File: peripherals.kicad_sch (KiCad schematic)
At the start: 9 parts

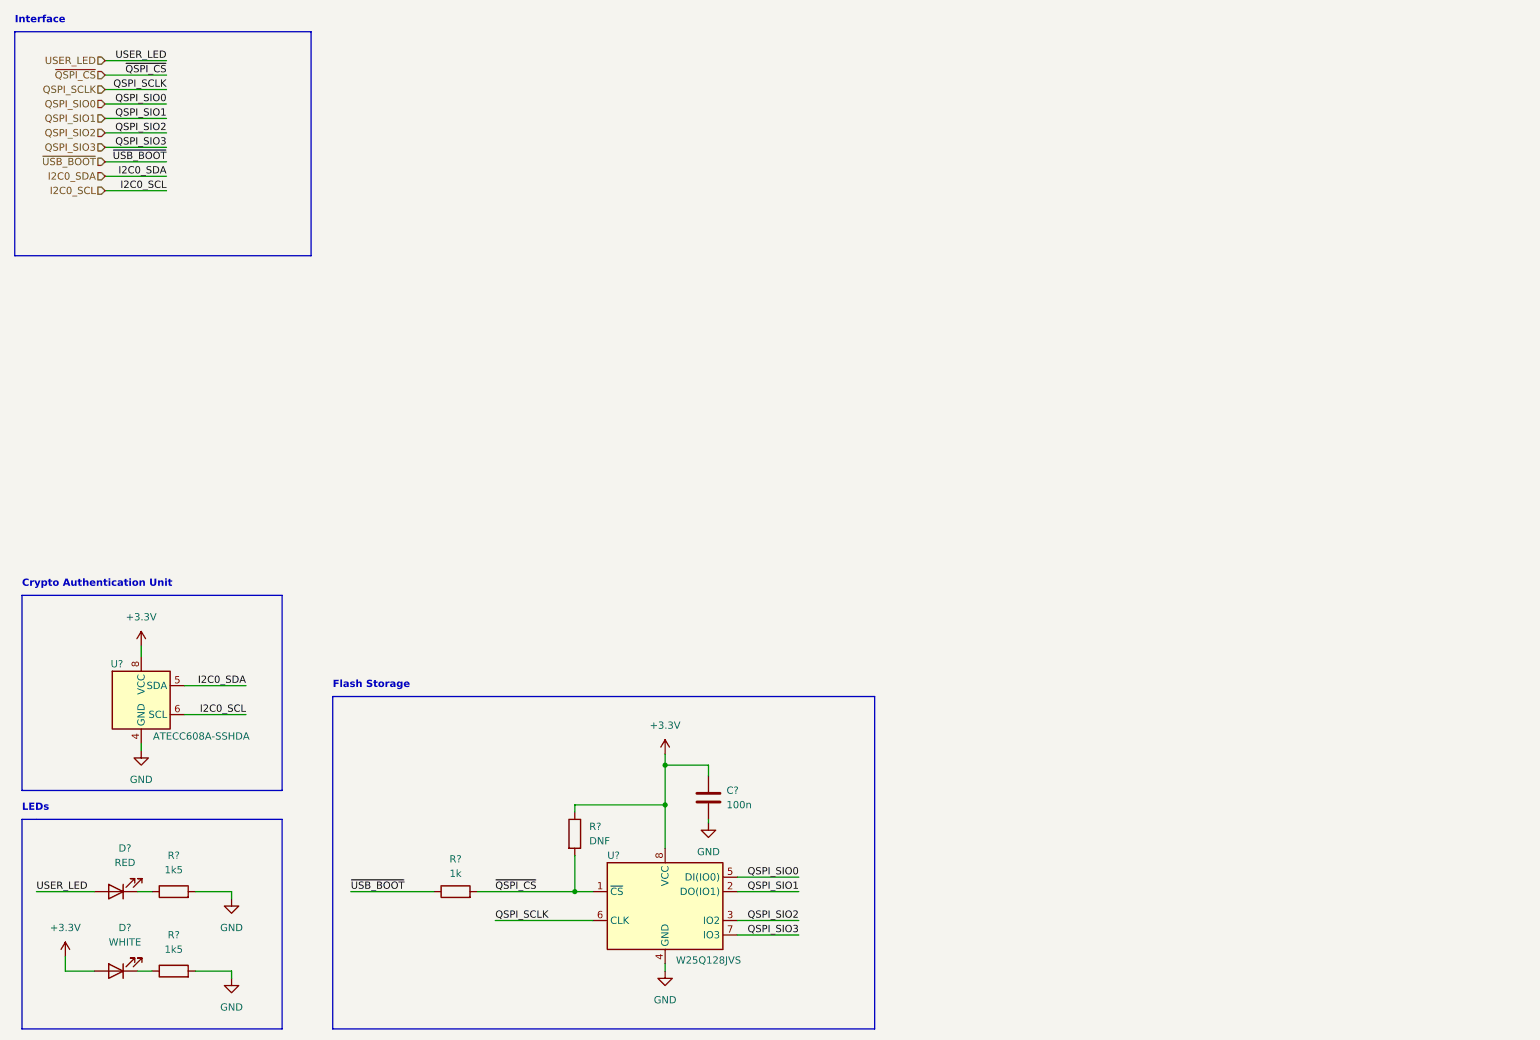
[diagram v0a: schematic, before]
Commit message: All component except led matrix
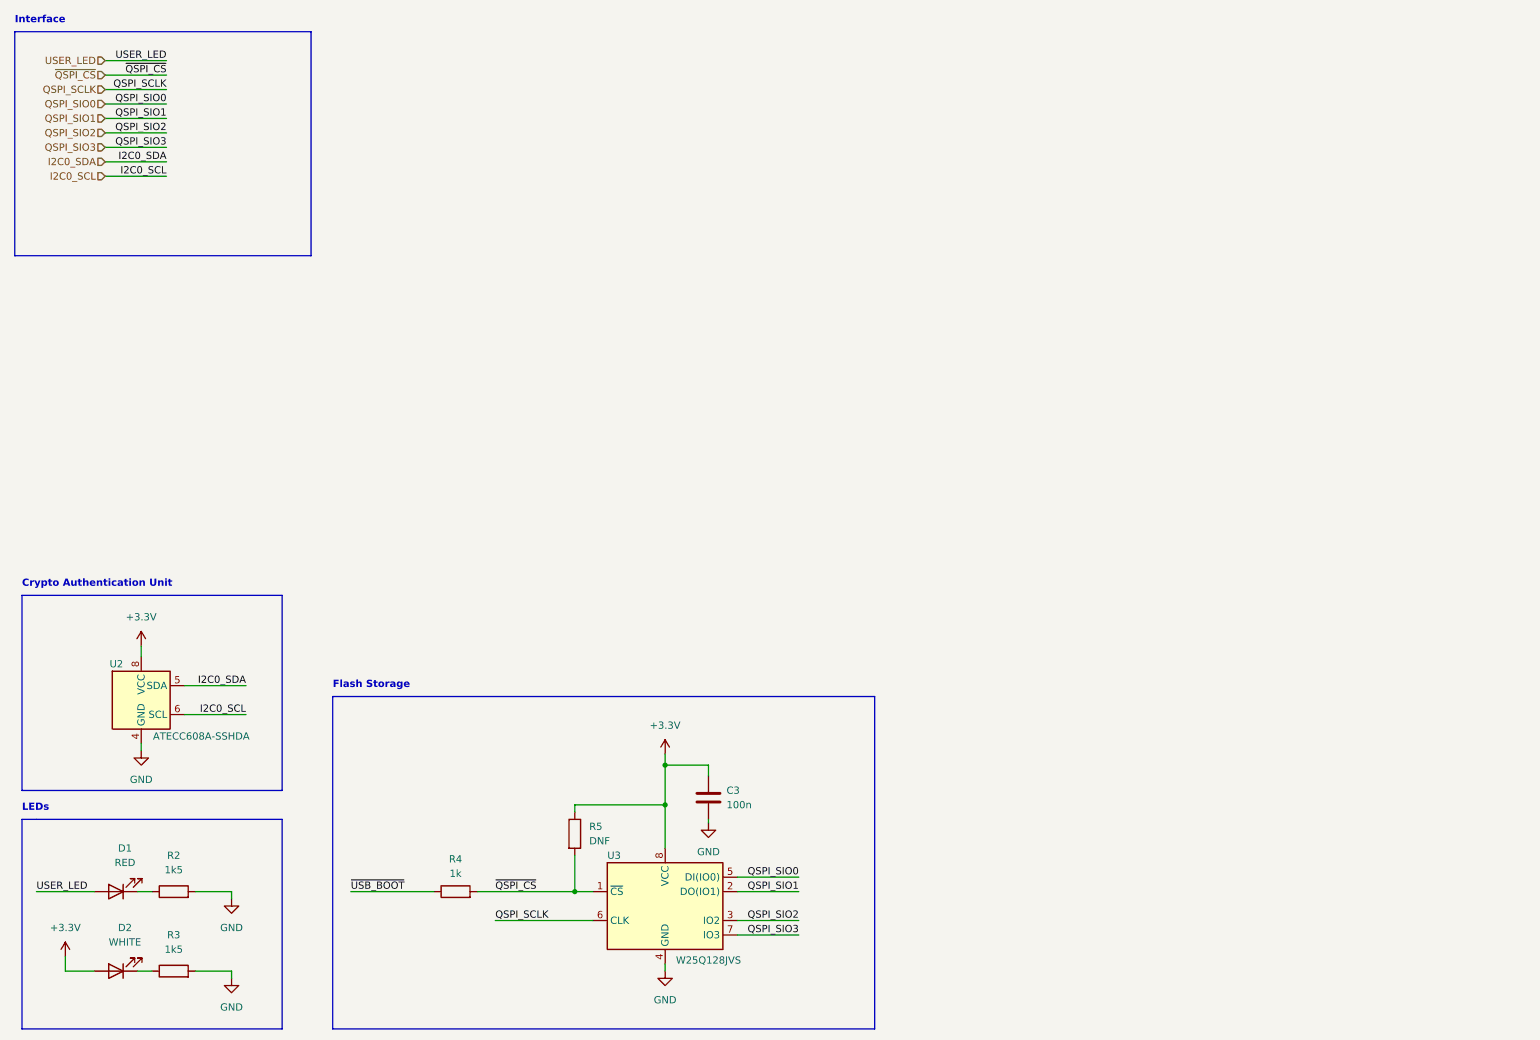
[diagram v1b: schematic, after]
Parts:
- gave numbers to parts that had none: 9
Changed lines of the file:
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@@
+    (stroke (width 0) (type default) (color 0 0 0 0))
+  )
+  (wire (pts (xy 31.115 41.91) (xy 41.91 41.91))
+    (stroke (width 0) (type default) (color 0 0 0 0))
+  )
+  (wire (pts (xy 31.115 39.37) (xy 41.91 39.37))
     (stroke (width 0) (type default) (color 0 0 0 0))
   )
@@
     (stroke (width 0) (type default) (color 0 0 0 0))
   )
-  (wire (pts (xy 31.115 39.37) (xy 41.91 39.37))
-    (stroke (width 0) (type default) (color 0 0 0 0))
-  )
-  (wire (pts (xy 31.115 46.99) (xy 41.91 46.99))
-    (stroke (width 0) (type default) (color 0 0 0 0))
-  )
   (wire (pts (xy 31.115 34.29) (xy 41.91 34.29))
     (stroke (width 0) (type default) (color 0 0 0 0))
@@
   )
   (wire (pts (xy 137.16 158.115) (xy 137.16 157.48))
-    (stroke (width 0) (type default) (color 0 0 0 0))
-  )
-  (wire (pts (xy 31.115 41.91) (xy 41.91 41.91))
     (stroke (width 0) (type default) (color 0 0 0 0))
   )
@@
     (effects (font (size 1.27 1.27)) (justify right bottom))
   )
-  (label "I2C0_SDA" (at 41.91 44.45 180)
+  (label "I2C0_SDA" (at 41.91 41.91 180)
     (effects (font (size 1.27 1.27)) (justify right bottom))
   )
@@
     (effects (font (size 1.27 1.27)) (justify right bottom))
   )
-  (label "I2C0_SCL" (at 41.91 46.99 180)
+  (label "I2C0_SCL" (at 41.91 44.45 180)
     (effects (font (size 1.27 1.27)) (justify right bottom))
   )
@@
   )
   (label "QSPI_SIO0" (at 41.91 31.75 180)
-    (effects (font (size 1.27 1.27)) (justify right bottom))
-  )
-  (label "~{USB_BOOT}" (at 41.91 41.91 180)
     (effects (font (size 1.27 1.27)) (justify right bottom))
   )
@@
     (effects (font (size 1.27 1.27)) (justify right))
   )
-  (hierarchical_label "I2C0_SDA" (shape input) (at 31.115 44.45 180)
+  (hierarchical_label "I2C0_SDA" (shape input) (at 31.115 41.91 180)
     (effects (font (size 1.27 1.27)) (justify right))
   )
@@
     (effects (font (size 1.27 1.27)) (justify right))
   )
-  (hierarchical_label "~{USB_BOOT}" (shape input) (at 31.115 41.91 180)
-    (effects (font (size 1.27 1.27)) (justify right))
-  )
   (hierarchical_label "QSPI_SIO3" (shape input) (at 31.115 39.37 180)
     (effects (font (size 1.27 1.27)) (justify right))
   )
-  (hierarchical_label "I2C0_SCL" (shape input) (at 31.115 46.99 180)
+  (hierarchical_label "I2C0_SCL" (shape input) (at 31.115 44.45 180)
     (effects (font (size 1.27 1.27)) (justify right))
   )
   (symbol (lib_id "Device:R") (at 43.18 184.15 90) (unit 1)
     (in_bom yes) (on_board yes) (fields_autoplaced)
-    (property "Reference" "R?" (id 0) (at 43.18 177.8 90))
+    (property "Reference" "R3" (id 0) (at 43.18 177.8 90))
     (property "Value" "1k5" (id 1) (at 43.18 180.34 90))
     (property "Footprint" "" (id 2) (at 43.18 185.928 90)
@@
   (symbol (lib_id "power:+3.3V") (at 37.465 127 0) (unit 1)
     (in_bom yes) (on_board yes) (fields_autoplaced)
-    (property "Reference" "#PWR?" (id 0) (at 37.465 130.81 0)
+    (property "Reference" "#PWR0131" (id 0) (at 37.465 130.81 0)
       (effects (font (size 1.27 1.27)) hide)
     )
@@
   (symbol (lib_id "Device:C") (at 137.16 153.67 0) (unit 1)
     (in_bom yes) (on_board yes) (fields_autoplaced)
-    (property "Reference" "C?" (id 0) (at 140.335 152.3999 0)
+    (property "Reference" "C3" (id 0) (at 140.335 152.3999 0)
       (effects (font (size 1.27 1.27)) (justify left))
     )
@@
   (symbol (lib_id "Security:ATECC608A-SSHDA") (at 37.465 136.525 0) (unit 1)
     (in_bom yes) (on_board yes)
-    (property "Reference" "U?" (id 0) (at 34.29 130.175 0)
+    (property "Reference" "U2" (id 0) (at 34.29 130.175 0)
       (effects (font (size 1.27 1.27)) (justify right))
     )
@@
   (symbol (lib_id "Device:LED") (at 33.02 184.15 180) (unit 1)
     (in_bom yes) (on_board yes) (fields_autoplaced)
-    (property "Reference" "D?" (id 0) (at 34.6075 176.53 0))
+    (property "Reference" "D2" (id 0) (at 34.6075 176.53 0))
     (property "Value" "WHITE" (id 1) (at 34.6075 179.07 0))
     (property "Footprint" "" (id 2) (at 33.02 184.15 0)
@@
   (symbol (lib_id "Device:R") (at 113.665 160.02 0) (unit 1)
     (in_bom yes) (on_board yes) (fields_autoplaced)
-    (property "Reference" "R?" (id 0) (at 116.205 158.7499 0)
+    (property "Reference" "R5" (id 0) (at 116.205 158.7499 0)
       (effects (font (size 1.27 1.27)) (justify left))
     )
@@
   (symbol (lib_id "Device:R") (at 43.18 170.18 90) (unit 1)
     (in_bom yes) (on_board yes) (fields_autoplaced)
-    (property "Reference" "R?" (id 0) (at 43.18 163.83 90))
+    (property "Reference" "R2" (id 0) (at 43.18 163.83 90))
     (property "Value" "1k5" (id 1) (at 43.18 166.37 90))
     (property "Footprint" "" (id 2) (at 43.18 171.958 90)
@@
   (symbol (lib_id "Memory_Flash:W25Q128JVS") (at 129.54 172.72 0) (unit 1)
     (in_bom yes) (on_board yes)
-    (property "Reference" "U?" (id 0) (at 119.38 163.83 0)
+    (property "Reference" "U3" (id 0) (at 119.38 163.83 0)
       (effects (font (size 1.27 1.27)) (justify left))
     )
@@
   (symbol (lib_id "Device:R") (at 92.71 170.18 90) (unit 1)
     (in_bom yes) (on_board yes) (fields_autoplaced)
-    (property "Reference" "R?" (id 0) (at 92.71 164.465 90))
+    (property "Reference" "R4" (id 0) (at 92.71 164.465 90))
     (property "Value" "1k" (id 1) (at 92.71 167.005 90))
     (property "Footprint" "" (id 2) (at 92.71 171.958 90)
@@
   (symbol (lib_id "Device:LED") (at 33.02 170.18 180) (unit 1)
     (in_bom yes) (on_board yes) (fields_autoplaced)
-    (property "Reference" "D?" (id 0) (at 34.6075 162.56 0))
+    (property "Reference" "D1" (id 0) (at 34.6075 162.56 0))
     (property "Value" "RED" (id 1) (at 34.6075 165.1 0))
     (property "Footprint" "" (id 2) (at 33.02 170.18 0)

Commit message: finish schematic, prep pcb
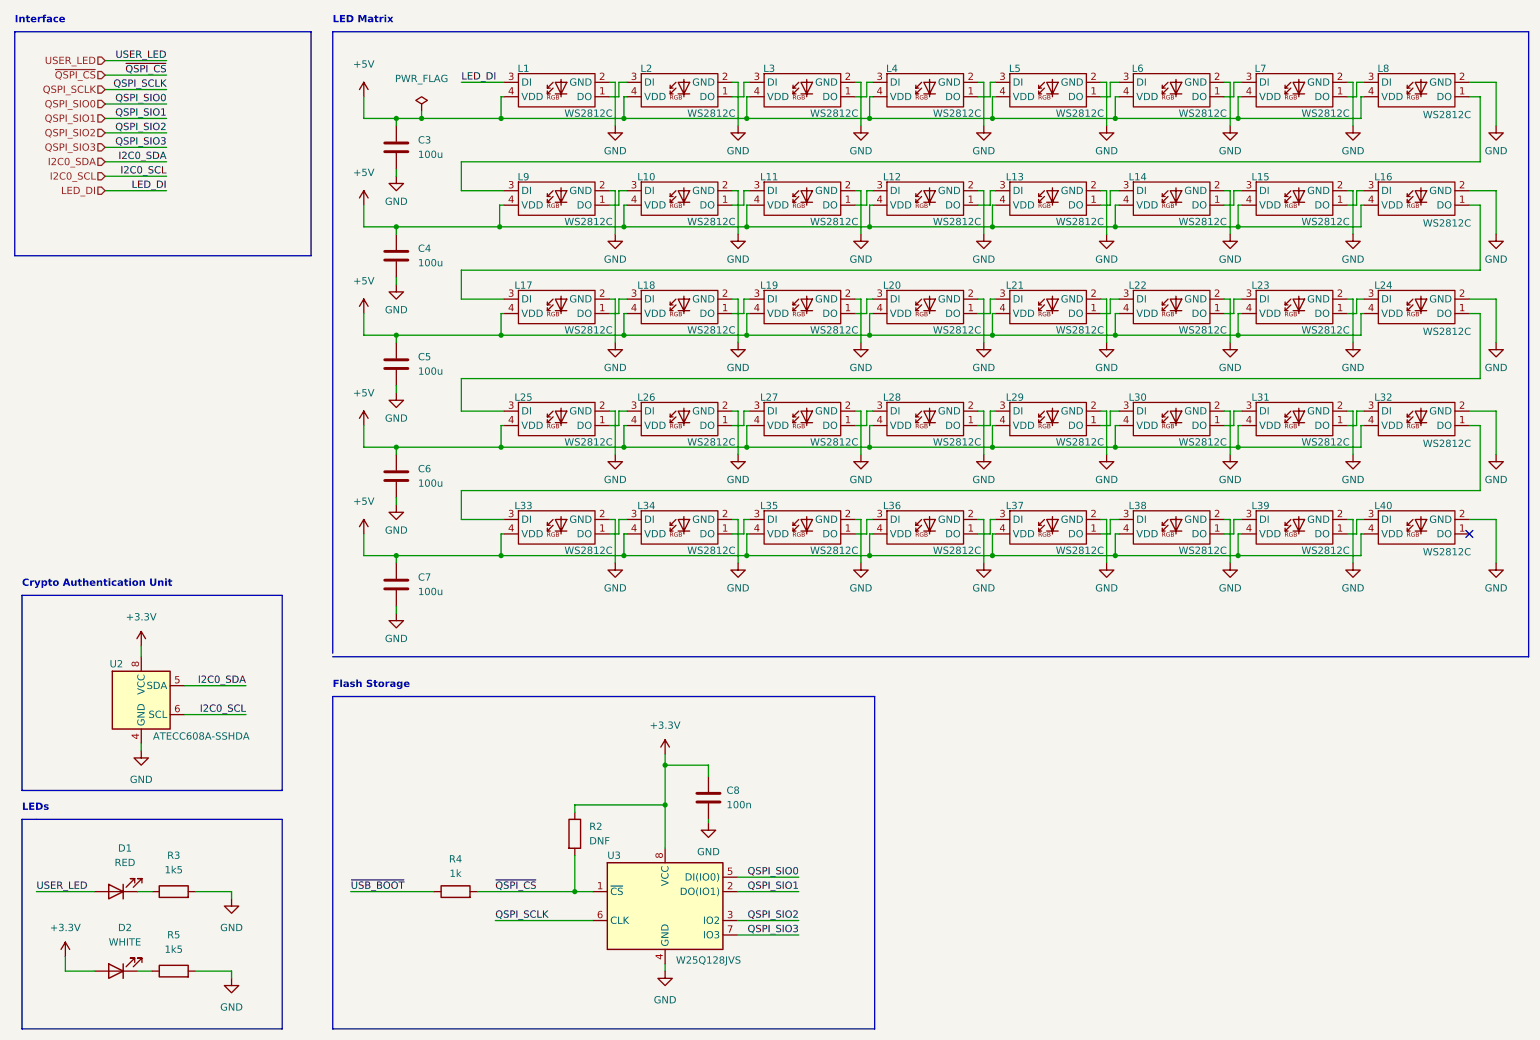
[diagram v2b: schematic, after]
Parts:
- added C3, C4, C5, C6, C7: 100u, Capacitor_SMD:C_1206_3216Metric, symbol Device:C
- added L1, L10, L11, L12, L13, L14, L15, L16, L17, L18, L19, L2, L20, L21, L22, L23, L24, L25, L26, L27, L28, L29, L3, L30, L31, L32, L33, L34, L35, L36, L37, L38, L39, L4, L40, L5, L6, L7, L8, L9: WS2812C, pico-card:WS2812C-2020, symbol pico-card:WS2812C
- C8: renamed from C3; footprint (none) -> Capacitor_SMD:C_0402_1005Metric
- D1, D2: footprint (none) -> LED_SMD:LED_0201_0603Metric
- R2: renamed from R5; footprint (none) -> Resistor_SMD:R_0402_1005Metric
- R3: renamed from R2; footprint (none) -> Resistor_SMD:R_0402_1005Metric
- R4: footprint (none) -> Resistor_SMD:R_0402_1005Metric
- R5: renamed from R3; footprint (none) -> Resistor_SMD:R_0402_1005Metric
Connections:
- net GND: now also C3.2, C4.2, C5.2, C6.2, C7.2, L1.2 (GND), L10.2 (GND), L11.2 (GND), L12.2 (GND), L13.2 (GND), L14.2 (GND), L15.2 (GND), L16.2 (GND), L17.2 (GND), L18.2 (GND), L19.2 (GND), L2.2 (GND), L20.2 (GND), L21.2 (GND), L22.2 (GND), L23.2 (GND), L24.2 (GND), L25.2 (GND), L26.2 (GND), L27.2 (GND), L28.2 (GND), L29.2 (GND), L3.2 (GND), L30.2 (GND), L31.2 (GND), L32.2 (GND), L33.2 (GND), L34.2 (GND), L35.2 (GND), L36.2 (GND), L37.2 (GND), L38.2 (GND), L39.2 (GND), L4.2 (GND), L40.2 (GND), L5.2 (GND), L6.2 (GND), L7.2 (GND), L8.2 (GND), L9.2 (GND)
- new net: L34.1 (DO), L35.3 (DI)
- new net: L33.1 (DO), L34.3 (DI)
- new net: L28.1 (DO), L29.3 (DI)
- new net: L27.1 (DO), L28.3 (DI)
- new net: L39.1 (DO), L40.3 (DI)
- new net: L38.1 (DO), L39.3 (DI)
- new net: L14.1 (DO), L15.3 (DI)
- new net: L13.1 (DO), L14.3 (DI)
- new net: L12.1 (DO), L13.3 (DI)
- new net: L6.1 (DO), L7.3 (DI)
- new net: L5.1 (DO), L6.3 (DI)
- new net: L30.1 (DO), L31.3 (DI)
- new net: L29.1 (DO), L30.3 (DI)
- new net: L18.1 (DO), L19.3 (DI)
- new net: L17.1 (DO), L18.3 (DI)
- new net: L8.1 (DO), L9.3 (DI)
- new net: L7.1 (DO), L8.3 (DI)
- new net: L2.1 (DO), L3.3 (DI)
- new net: L1.1 (DO), L2.3 (DI)
- new net: L32.1 (DO), L33.3 (DI)
- new net: L31.1 (DO), L32.3 (DI)
- new net: L21.1 (DO), L22.3 (DI)
- new net: L20.1 (DO), L21.3 (DI)
- new net: L23.1 (DO), L24.3 (DI)
- new net: L22.1 (DO), L23.3 (DI)
- new net: L19.1 (DO), L20.3 (DI)
- new net: L26.1 (DO), L27.3 (DI)
- new net: L25.1 (DO), L26.3 (DI)
- new net: L3.1 (DO), L4.3 (DI)
- new net: L10.1 (DO), L11.3 (DI)
- new net: L10.3 (DI), L9.1 (DO)
- new net: L35.1 (DO), L36.3 (DI)
- new net: L16.1 (DO), L17.3 (DI)
- new net: L15.1 (DO), L16.3 (DI)
- new net: L4.1 (DO), L5.3 (DI)
- new net: L11.1 (DO), L12.3 (DI)
- new net: L24.1 (DO), L25.3 (DI)
- new net: L37.1 (DO), L38.3 (DI)
- new net: L36.1 (DO), L37.3 (DI)
- new net +5V: C3.1, C4.1, C5.1, C6.1, C7.1, L1.4 (VDD), L10.4 (VDD), L11.4 (VDD), L12.4 (VDD), L13.4 (VDD), L14.4 (VDD), L15.4 (VDD), L16.4 (VDD), L17.4 (VDD), L18.4 (VDD), L19.4 (VDD), L2.4 (VDD), L20.4 (VDD), L21.4 (VDD), L22.4 (VDD), L23.4 (VDD), L24.4 (VDD), L25.4 (VDD), L26.4 (VDD), L27.4 (VDD), L28.4 (VDD), L29.4 (VDD), L3.4 (VDD), L30.4 (VDD), L31.4 (VDD), L32.4 (VDD), L33.4 (VDD), L34.4 (VDD), L35.4 (VDD), L36.4 (VDD), L37.4 (VDD), L38.4 (VDD), L39.4 (VDD), L4.4 (VDD), L40.4 (VDD), L5.4 (VDD), L6.4 (VDD), L7.4 (VDD), L8.4 (VDD), L9.4 (VDD)
- new net LED_DI: L1.3 (DI)
- no-connect marks 0 -> 1
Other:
- note added: "LED Matrix"
